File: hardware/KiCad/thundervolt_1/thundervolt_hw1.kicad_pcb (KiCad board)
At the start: 4 copper layers, 46.9 x 54.8 mm, 59 parts, among them IC4 LP5907UVX-1.8_NOPB, U1 TPS628681ARQYR, U2 TPS628681ARQYR, U3 TPS628682ARQYR, U4 TPS63810YFFR, U5 ATTINY1616-MNR, U7 TMP1075NDRLR

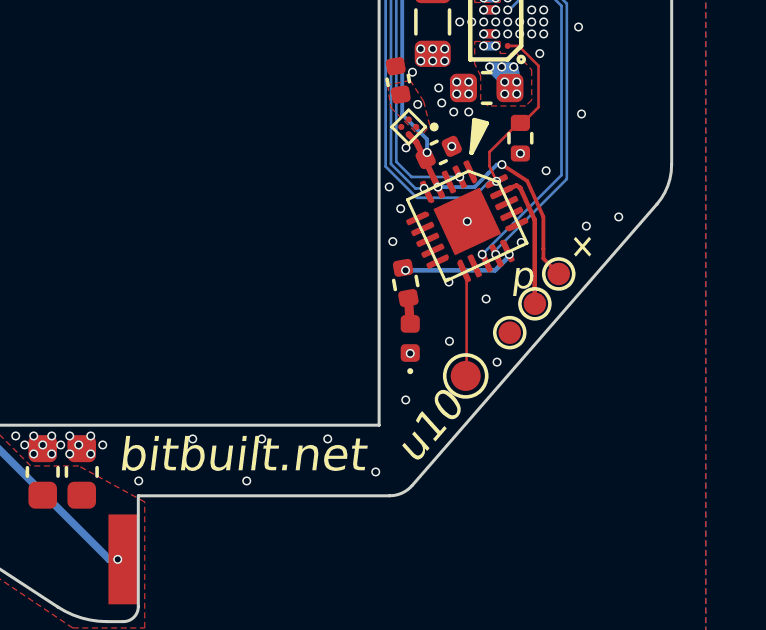
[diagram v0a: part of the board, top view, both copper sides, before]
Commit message: U10 FET Mode
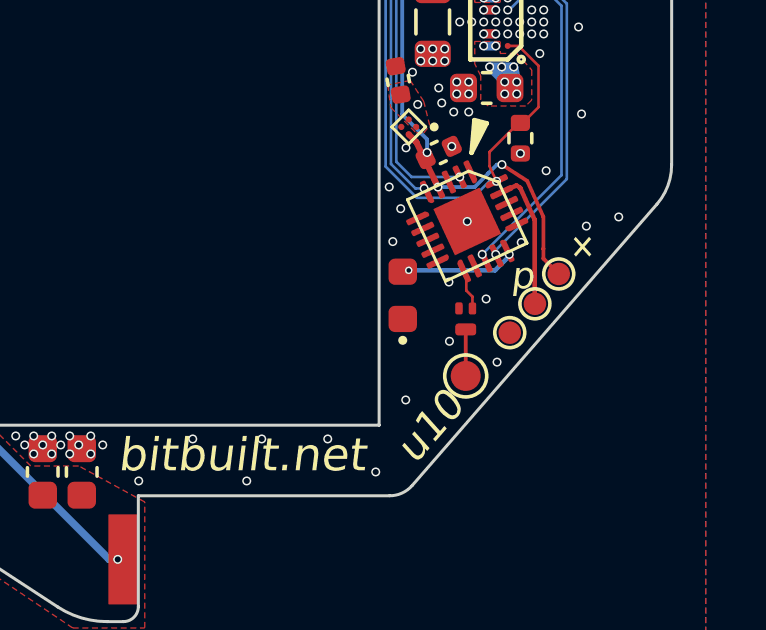
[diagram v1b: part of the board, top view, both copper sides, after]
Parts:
- removed R6: 0Ω, Resistor_SMD:R_0402_1005Metric
- added Q1: NX7002BKMYL, Package_DFN_QFN:Diodes_DFN1006-3, F.Cu at (158.6, 117.6)
- D1: footprint LED_SMD:LED_0402_1005Metric -> SamacSys_Parts:LED_0603_1608Metric
- moved D1 1.46 mm to (156.5, 116.8)
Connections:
- U5 pad 11: U10 -> Net-(Q1-G)
- U5 pad 15: Net-(U5-PC0) -> Net-(D1-A)
- U5 pad 8: unconnected-(U5-PA7-Pad8) -> GND
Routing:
- net Net-(U5-PC0): track 3.98 -> 0.00 mm, vias 2 -> 0
- net Net-(D1-A): track 0.86 -> 3.75 mm, vias 0 -> 2
- net U10: track 3.55 -> 1.64 mm
- net Net-(Q1-G): track 0.00 -> 1.50 mm
- net GND: vias 278 -> 277
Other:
- copper layers 4 -> 13
